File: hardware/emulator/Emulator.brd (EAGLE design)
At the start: 69.6 x 71 mm, 41 parts, among them T1 VP0109N3, T2 2N5401, U1 DEV-16771_REDUCED_PINS, U2 OPA2277PA, U3 MCP4822-E/P, U4 LM6132BIN, U5 L7808ABV, U6 L7908CV

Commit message: Add minor changes to the hardware
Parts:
- added T3: 2N5401, transistor-neu-to92:TO92-EBC
- R1, R2: value 1k5 -> 1k
- R3, R4: value 470k -> 499k
- T2: value 2N5401 -> IRF9530PBF; device transistor-neu-to92:TO92-EBC -> IRF9530PBF:TO220AB_VIS
- moved T2 34.6 mm to (58.9, 34.5), turned to 0 degrees
- moved EMULATOR_TERMINAL 3.05 mm to (62.5, 23.4)
- moved C8 3.05 mm to (61.2, 16.1)
- moved T1 1.98 mm to (61.7, 41.1), turned to 180 degrees
- moved C5 0.51 mm to (27.9, 15.7)
- moved C6 0.51 mm to (25.4, 15.7)
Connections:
- net GND: now also T3.C; no longer T2.C
- net HARVESTER_EMULATION: now also T2.D, T3.E; no longer T2.E
- net N$12: now also T3.B; no longer T2.B
- net N$5: now also T2.G
- net N$7: now also T2.S
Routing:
- net HARVESTER_EMULATION: track 70.2 -> 87.1 mm
- net N$7: track 16.0 -> 31.7 mm
- net N$5: track 11.4 -> 20.1 mm

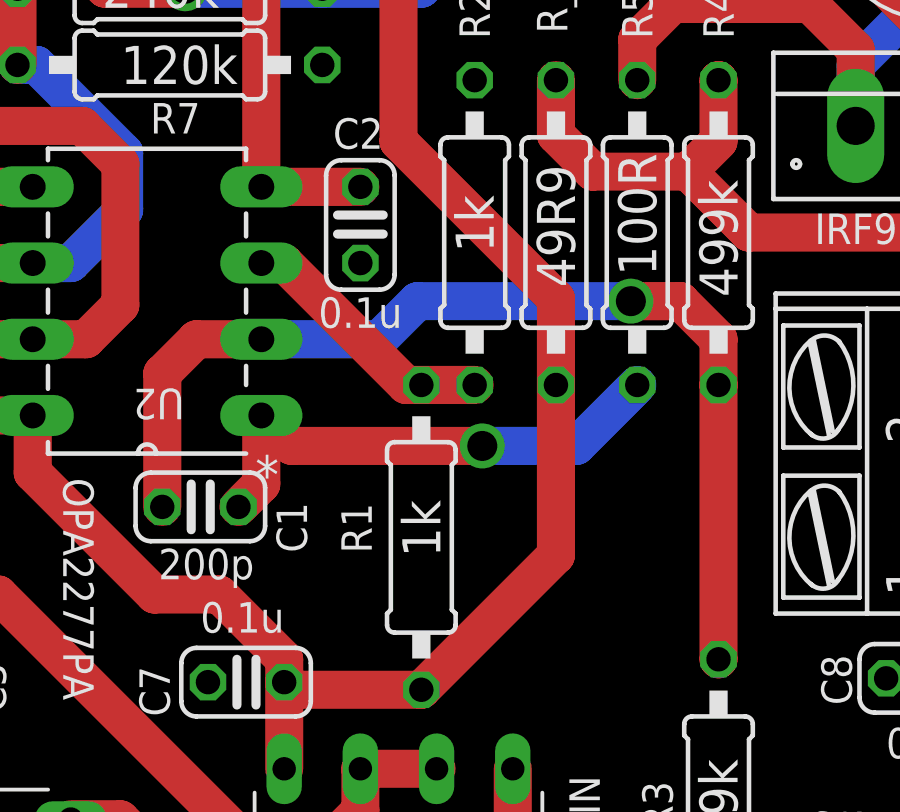
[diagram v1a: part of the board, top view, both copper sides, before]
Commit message: Update resistor value
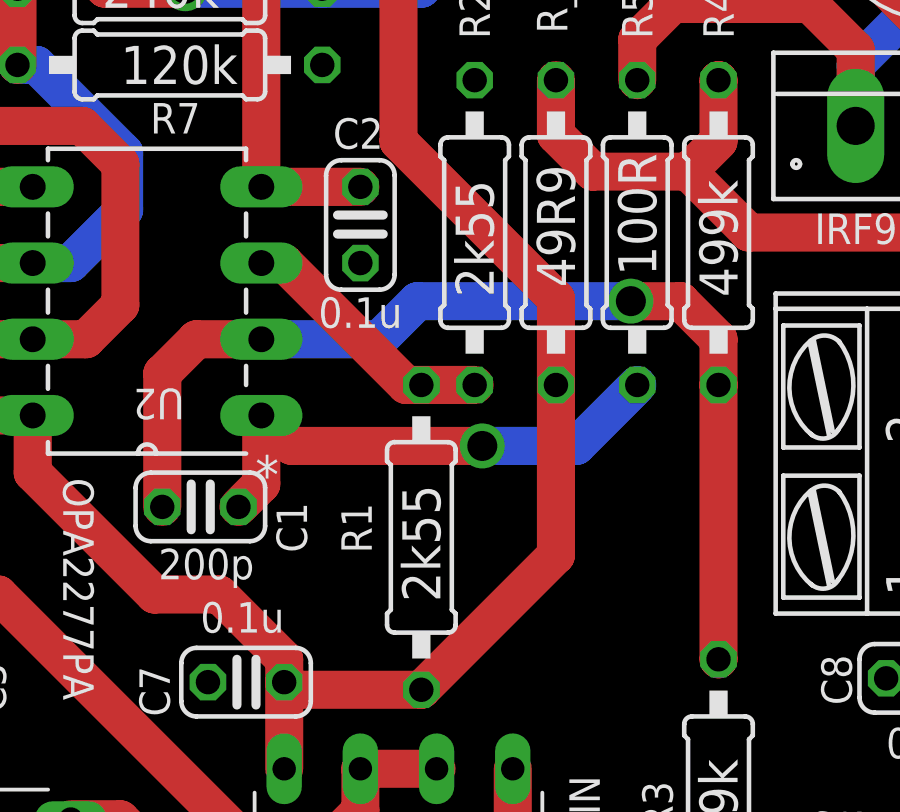
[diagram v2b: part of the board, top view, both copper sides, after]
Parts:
- R1, R2: value 1k -> 2k55
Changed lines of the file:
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@@
 <drawing>
 <settings>
-<setting alwaysvectorfont="yes"/>
+<setting alwaysvectorfont="no"/>
 <setting verticaltext="up"/>
 </settings>
@@
 <attribute name="VENDOR" value="Texas Instruments" x="63.5" y="31.496" size="1.778" layer="27" rot="R180" display="off"/>
 </element>
-<element name="R1" library="rcl" library_urn="urn:adsk.eagle:library:334" package="0207/10" package3d_urn="urn:adsk.eagle:package:23491/2" value="1k" x="44.45" y="20.828" smashed="yes" rot="R270">
+<element name="R1" library="rcl" library_urn="urn:adsk.eagle:library:334" package="0207/10" package3d_urn="urn:adsk.eagle:package:23491/2" value="2k55" x="44.45" y="20.828" smashed="yes" rot="R270">
 <attribute name="NAME" x="41.783" y="21.971" size="1.016" layer="25" ratio="10" rot="R270"/>
 <attribute name="POPULARITY" value="81" x="63.246" y="40.64" size="1.778" layer="27" rot="R270" display="off"/>
 <attribute name="SPICEPREFIX" value="R" x="63.246" y="40.64" size="1.778" layer="27" rot="R270" display="off"/>
-<attribute name="VALUE" x="43.815" y="22.0726" size="1.27" layer="25" ratio="10" rot="R270"/>
+<attribute name="VALUE" x="43.815" y="22.5806" size="1.27" layer="25" ratio="10" rot="R270"/>
 </element>
-<element name="R2" library="rcl" library_urn="urn:adsk.eagle:library:334" package="0207/10" package3d_urn="urn:adsk.eagle:package:23491/2" value="1k" x="46.228" y="30.988" smashed="yes" rot="R270">
+<element name="R2" library="rcl" library_urn="urn:adsk.eagle:library:334" package="0207/10" package3d_urn="urn:adsk.eagle:package:23491/2" value="2k55" x="46.228" y="30.988" smashed="yes" rot="R270">
 <attribute name="NAME" x="45.72" y="39.116" size="1.016" layer="25" ratio="10" rot="R270"/>
 <attribute name="POPULARITY" value="81" x="60.452" y="62.484" size="1.778" layer="27" rot="R270" display="off"/>
 <attribute name="SPICEPREFIX" value="R" x="60.452" y="62.484" size="1.778" layer="27" rot="R270" display="off"/>
-<attribute name="VALUE" x="45.593" y="32.2326" size="1.27" layer="25" ratio="10" rot="R270"/>
+<attribute name="VALUE" x="45.593" y="32.7406" size="1.27" layer="25" ratio="10" rot="R270"/>
 </element>
 <element name="R3" library="rcl" library_urn="urn:adsk.eagle:library:334" package="0207/10" package3d_urn="urn:adsk.eagle:package:23491/2" value="499k" x="54.356" y="11.684" smashed="yes" rot="R270">
